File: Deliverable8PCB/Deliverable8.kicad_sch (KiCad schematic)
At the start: 55 parts, among them J2 PiHeaderM, Q1 NMOS, Q2 PMOS, U1 MCP4131-xxxx-P, U10 MCP4131-xxxx-P, U11 MCP4131-xxxx-P, U12 LM741, U2 LM741, U3 LM741, U4 LM339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

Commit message: update i2c_lcd
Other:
- note added: "Square Wave/ DC Reference Design"
- note removed: "Sqaure Wave/ DC Reference Design"
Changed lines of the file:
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@@
 		)
 	)
-	(text "Sqaure Wave/ DC Reference Design"
+	(text "Square Wave/ DC Reference Design"
 		(exclude_from_sim no)
 		(at 353.06 309.88 0)

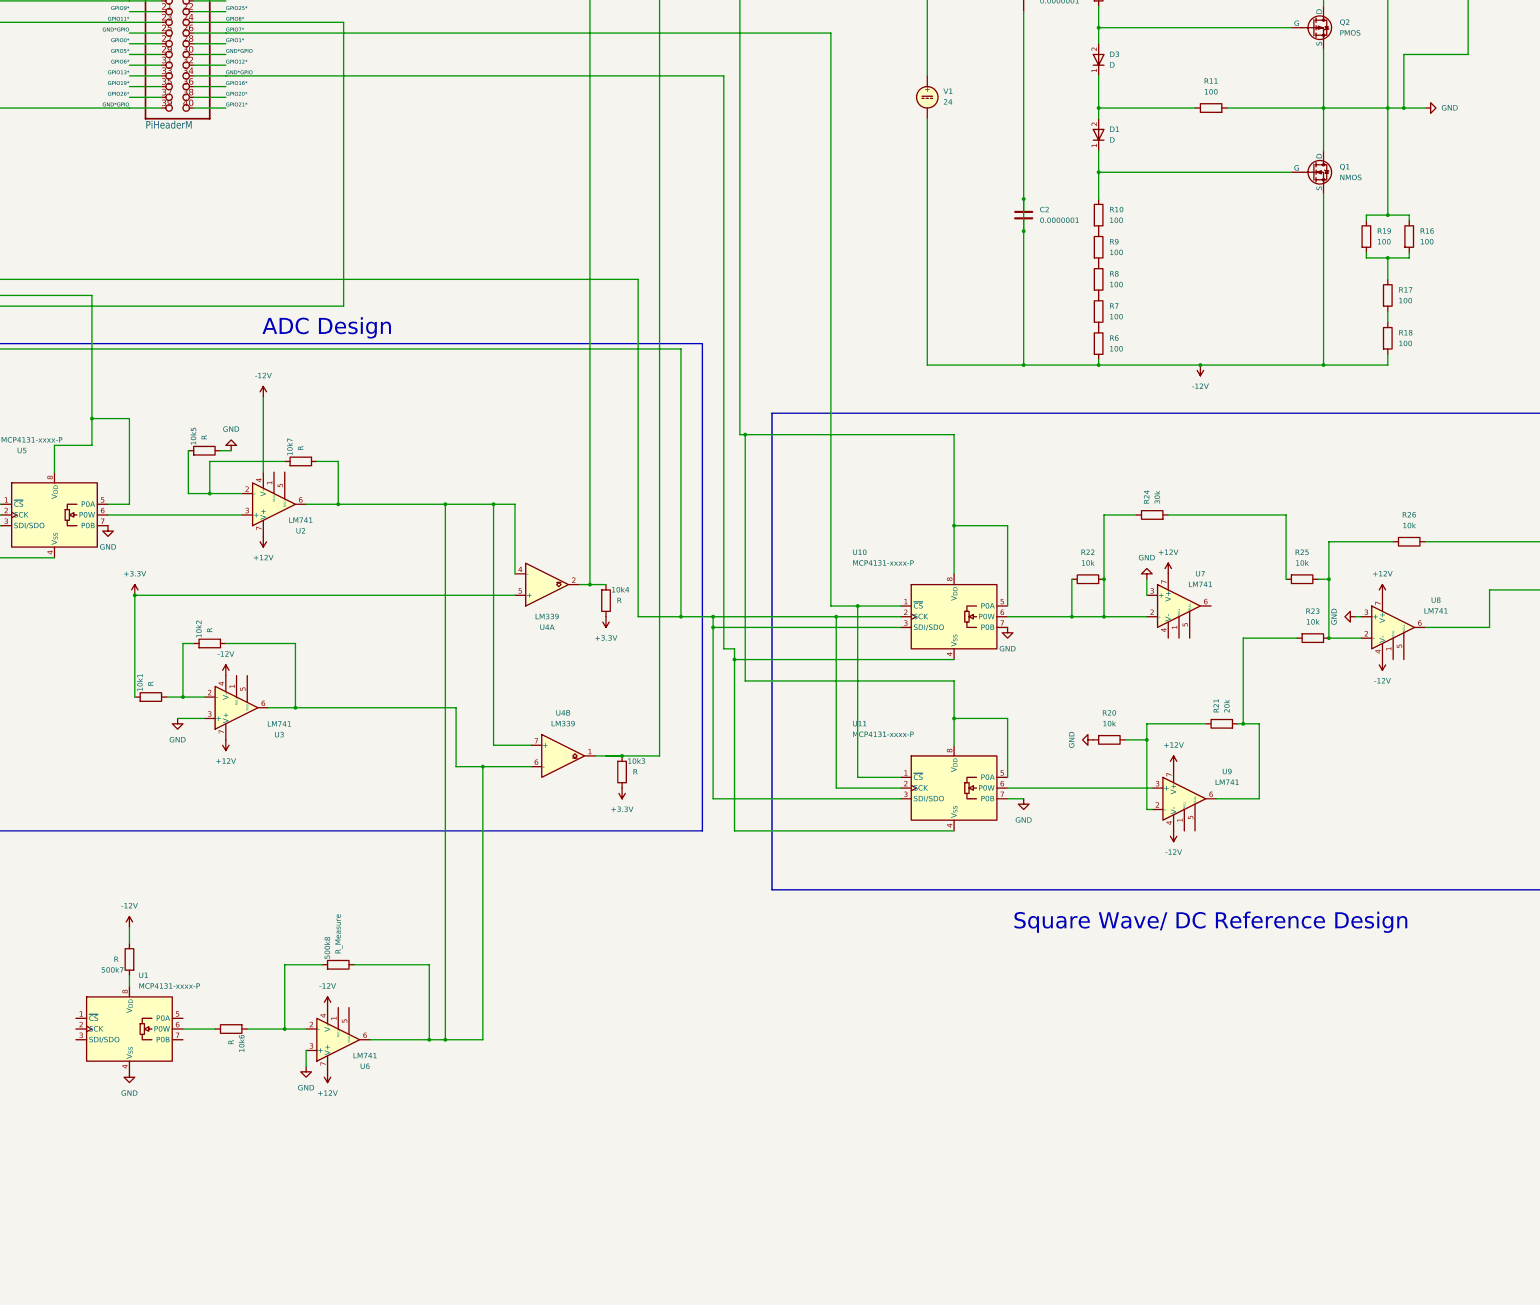
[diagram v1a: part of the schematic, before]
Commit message: added voltmeter
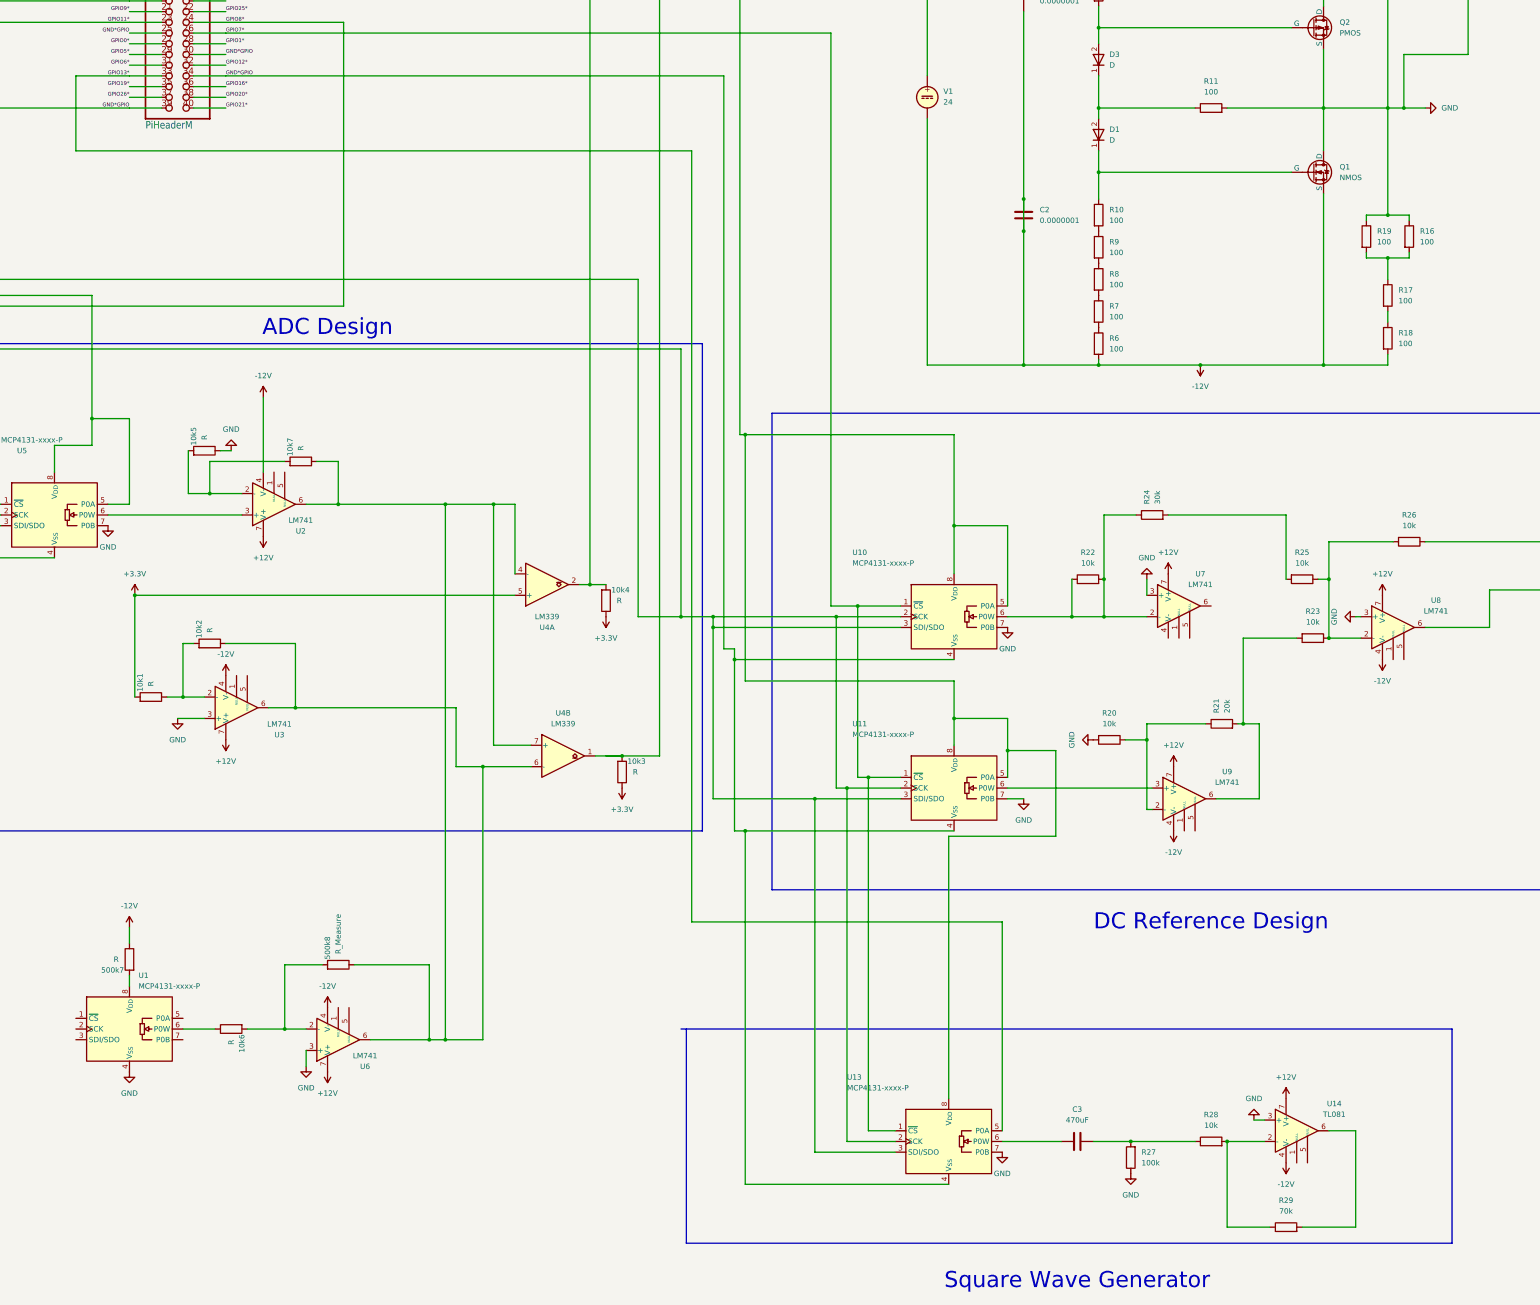
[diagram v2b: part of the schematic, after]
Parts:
- added C3: 470uF, Capacitor_SMD:CP_Elec_3x5.3, symbol Device:C
- added R27: 100k, Resistor_SMD:R_0201_0603Metric, symbol Device:R
- added R28: 10k, Resistor_SMD:R_0201_0603Metric, symbol Device:R
- added R29: 70k, Resistor_SMD:R_0201_0603Metric, symbol Device:R
- added U13: MCP4131-xxxx-P, Package_DIP:DIP-8_W7.62mm, symbol Potentiometer_Digital:MCP4131-xxxx-P
- added U14: TL081, Package_DIP:DIP-8_W7.62mm, symbol Amplifier_Operational:TL081
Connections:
- net +12V: now also U14.7 (V+)
- net -12V: now also U14.4 (V-)
- net 3V3GPIO*: now also U13.8 (V_{DD})
- net GND: now also R27.1, U13.4 (V_{SS}), U13.7 (P0B), U14.3 (+)
- net GPIO10*: now also U13.2 (SCK), U13.3 (SDI/SDO)
- net GPIO13*: now also U13.5 (P0A)
- net GPIO7*: now also U13.1 (~{CS})
- new net: C3.1, R27.2, R28.1
- new net: C3.2, U13.6 (P0W)
- new net: R28.2, R29.1, U14.2 (-)
- new net: R29.2, U14.6
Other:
- note added: "DC Reference Design"
- note added: "Square Wave Generator"
- note removed: "Square Wave/ DC Reference Design"

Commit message: added turn off feature
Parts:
- U14: footprint Package_DIP:DIP-8_W7.62mm -> (none)
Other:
- note added: "Ohmmeter"
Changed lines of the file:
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@@
 		)
 	)
+	(text "Ohmmeter"
+		(exclude_from_sim no)
+		(at 119.38 368.3 0)
+		(effects
+			(font
+				(size 3.81 3.81)
+			)
+		)
+	)
 	(text "Square Wave Generator"
 		(exclude_from_sim no)
@@
 		)
 	)
+	(polyline
+		(pts
+			(xy 189.23 359.41) (xy 57.15 359.41)
+		)
+		(stroke
+			(width 0)
+			(type default)
+		)
+	)
 	(wire
 		(pts
@@
 		)
 	)
+	(polyline
+		(pts
+			(xy 57.15 300.99) (xy 189.23 300.99)
+		)
+		(stroke
+			(width 0)
+			(type default)
+		)
+	)
 	(wire
 		(pts
@@
 		)
 	)
+	(polyline
+		(pts
+			(xy 57.15 300.99) (xy 57.15 359.41)
+		)
+		(stroke
+			(width 0)
+			(type default)
+		)
+	)
 	(wire
 		(pts
@@
 		)
 	)
+	(polyline
+		(pts
+			(xy 189.23 300.99) (xy 189.23 359.41)
+		)
+		(stroke
+			(width 0)
+			(type default)
+		)
+	)
 	(wire
 		(pts
@@
 			)
 		)
-		(property "Footprint" "Package_DIP:DIP-8_W7.62mm"
+		(property "Footprint" ""
 			(at 374.65 358.14 0)
 			(effects
